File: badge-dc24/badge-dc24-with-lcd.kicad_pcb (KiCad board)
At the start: 2 copper layers, 26 parts, among them U1 ESP-12E, U2 TSOP38238, U3 74HC595

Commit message: Almost there
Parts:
- moved Program1 34.9 mm to (87.9, 116.9), turned to 180 degrees
- moved L1 22.4 mm to (86.9, 91.9)
- moved L2 22.4 mm to (84.3, 91.9)
- moved L3 22.4 mm to (81.8, 91.9)
- moved L5 22.4 mm to (76.7, 91.9)
- moved R3 22.4 mm to (76.7, 97.0)
- moved R5 22.4 mm to (81.8, 97.0)
- moved R6 22.4 mm to (84.3, 97.0)
- moved R7 22.4 mm to (86.9, 97.0)
- moved L4 22.4 mm to (79.2, 91.9)
- moved R4 22.4 mm to (79.2, 97.0)
- moved D1 21.4 mm to (91.1, 94.0)
- moved LCD1 20.9 mm to (102.4, 105.7), turned to 180 degrees
- moved U3 19.9 mm to (88.1, 81.7)
- moved Power2 19.8 mm to (77.3, 102.1)
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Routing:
- net Net-(LCD1-Pad4): track 49.2 -> 107.7 mm, vias 1 -> 0
- net Net-(Program1-Pad2): track 29.1 -> 62.7 mm
- net Net-(U1-Pad4): track 32.2 -> 52.1 mm
- net Net-(U1-Pad6): track 37.6 -> 57.5 mm
- net Net-(U1-Pad5): track 33.5 -> 52.6 mm
- net Net-(LCD1-Pad3): track 21.2 -> 37.8 mm
- net Net-(LCD1-Pad5): track 30.1 -> 43.4 mm
- net Net-(Infrared1-Pad2): track 41.5 -> 54.2 mm
- net GND: track 31.7 -> 41.4 mm
- net Net-(U1-Pad7): track 9.63 -> 18.3 mm
- net Net-(PROGRAM1-Pad1): track 28.0 -> 31.2 mm
- net Net-(RESET1-Pad2): track 13.6 -> 16.7 mm
- net Net-(L5-Pad1): track 17.5 -> 15.0 mm
- net Net-(D1-Pad4): track 6.55 -> 8.83 mm
- net Net-(D1-Pad3): track 7.08 -> 9.36 mm
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
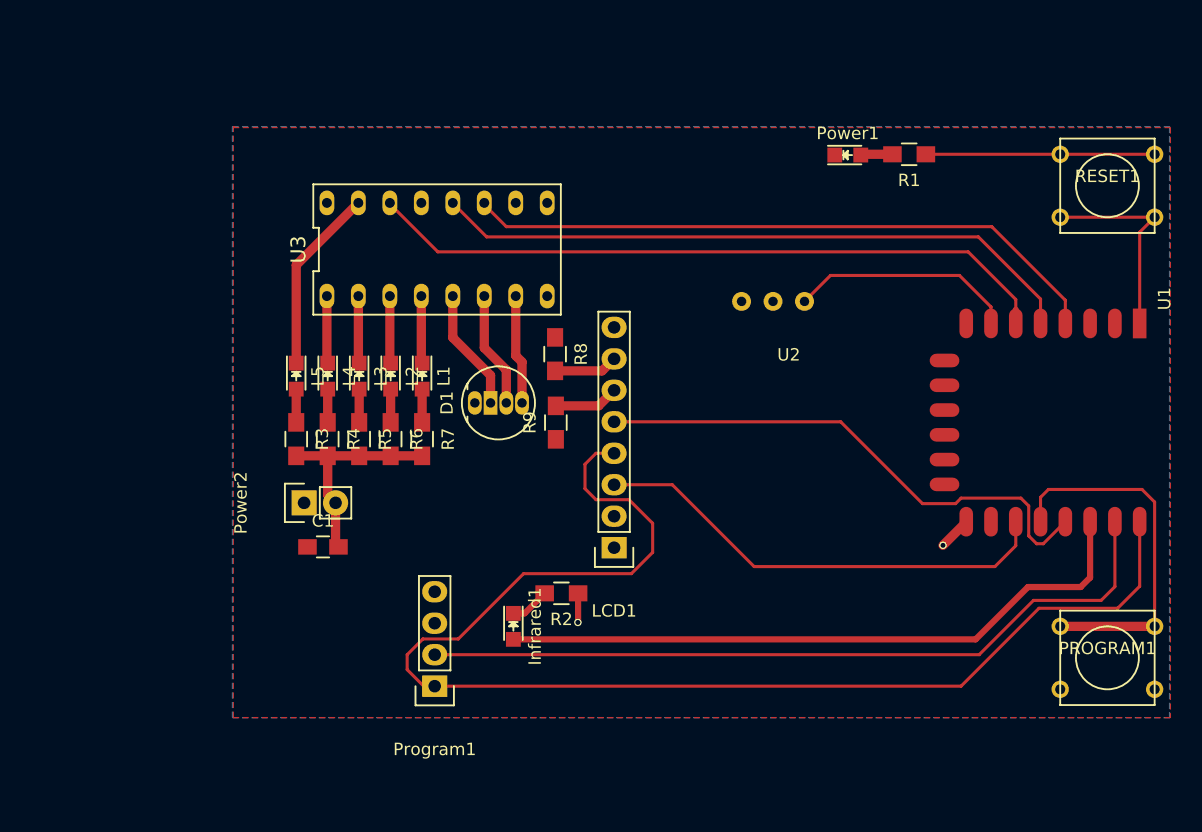
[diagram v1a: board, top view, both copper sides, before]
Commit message: Moved components out from under LCD
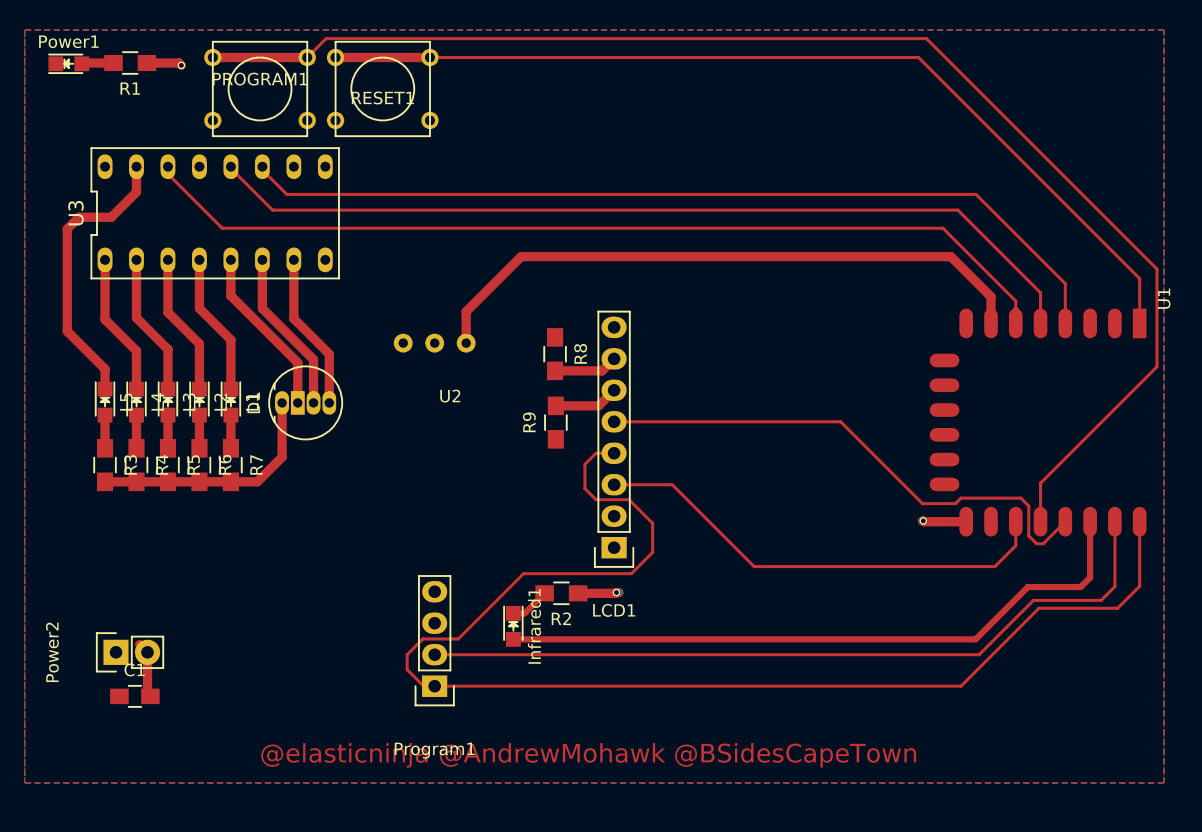
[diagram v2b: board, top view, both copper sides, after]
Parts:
- moved PROGRAM1 82.4 mm to (73.8, 68.7)
- moved Power1 63.3 mm to (58.4, 66.7)
- moved R1 63.3 mm to (63.3, 66.6)
- moved RESET1 59.0 mm to (83.7, 68.7), turned to 180 degrees
- moved U2 27.5 mm to (89.2, 93.0)
- moved C1 19.4 mm to (63.7, 117.7)
- moved Power2 19.4 mm to (62.2, 114.2)
- moved U3 18.1 mm to (70.2, 78.7)
- moved L2 15.6 mm to (68.9, 94.0)
- moved R6 15.6 mm to (68.9, 99.1)
- moved L4 15.6 mm to (63.8, 94.0)
- moved R4 15.6 mm to (63.8, 99.1)
- moved L1 15.6 mm to (71.4, 94.0)
- moved L3 15.6 mm to (66.4, 94.0)
- moved L5 15.6 mm to (61.3, 94.0)
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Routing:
- net Net-(PROGRAM1-Pad1): track 31.2 -> 110.5 mm
- net Net-(RESET1-Pad2): track 16.7 -> 75.9 mm
- net Net-(U1-Pad7): track 18.3 -> 50.2 mm
- net Net-(U1-Pad4): track 52.1 -> 72.1 mm
- net Net-(U1-Pad5): track 52.6 -> 72.1 mm
- net Net-(U1-Pad6): track 57.5 -> 76.8 mm
- net Net-(L5-Pad1): track 15.0 -> 23.1 mm
- net GND: track 41.4 -> 33.8 mm, vias 2 -> 3
- net Net-(L1-Pad1): track 5.44 -> 11.6 mm
- net Net-(L3-Pad1): track 5.44 -> 11.6 mm
- net Net-(L4-Pad1): track 5.44 -> 11.6 mm
- net Net-(L2-Pad1): track 5.44 -> 11.6 mm
- net Net-(D1-Pad3): track 9.36 -> 13.3 mm
- net Net-(D1-Pad4): track 8.83 -> 12.7 mm
- net Net-(D1-Pad2): track 9.89 -> 13.8 mm
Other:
- board text added: "@elasticninja @AndrewMohawk @BSidesCapeTown"

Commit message: Moved IR LED to the corner, for neatness' sake
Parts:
- moved Infrared1 48.0 mm to (141.4, 121.3), turned to 0 degrees
- moved R2 39.7 mm to (136.0, 121.3), turned to 0 degrees
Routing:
- net Net-(Infrared1-Pad2): track 54.2 -> 30.2 mm
- net GND: track 33.8 -> 32.2 mm
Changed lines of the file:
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@@
     (thickness 1.6)
     (drawings 5)
-    (tracks 154)
+    (tracks 152)
     (zones 0)
     (modules 26)
@@
   )
   (module LEDs:LED_0805 (layer F.Cu)
-    (at 94.234 112.0775 270)
+    (at 141.351 121.3485)
     (descr "LED 0805 smd package")
     (tags "LED 0805 SMD")
     (attr smd)
-    (fp_text reference Infrared1 (at 0 -1.75 270) (layer F.SilkS)
-      (effects (font (size 1 1) (thickness 0.15)))
-    )
-    (fp_text value LED (at 0 1.75 270) (layer F.Fab)
+    (fp_text reference Infrared1 (at 0 -1.75) (layer F.SilkS)
+      (effects (font (size 1 1) (thickness 0.15)))
+    )
+    (fp_text value LED (at 0 1.75) (layer F.Fab)
       (effects (font (size 1 1) (thickness 0.15)))
     )
@@
     (fp_line (start -1.9 0.95) (end -1.9 -0.95) (layer F.CrtYd) (width 0.05))
     (fp_line (start -1.9 -0.95) (end 1.9 -0.95) (layer F.CrtYd) (width 0.05))
-    (pad 2 smd rect (at 1.04902 0 90) (size 1.19888 1.19888) (layers F.Cu F.Paste F.Mask)
+    (pad 2 smd rect (at 1.04902 0 180) (size 1.19888 1.19888) (layers F.Cu F.Paste F.Mask)
       (net 17 "Net-(Infrared1-Pad2)"))
-    (pad 1 smd rect (at -1.04902 0 90) (size 1.19888 1.19888) (layers F.Cu F.Paste F.Mask)
+    (pad 1 smd rect (at -1.04902 0 180) (size 1.19888 1.19888) (layers F.Cu F.Paste F.Mask)
       (net 36 "Net-(Infrared1-Pad1)"))
     (model LEDs.3dshapes/LED_0805.wrl
@@
   )
   (module Resistors_SMD:R_0805_HandSoldering (layer F.Cu)
-    (at 98.1075 109.4105 180)
+    (at 135.9535 121.3485)
     (descr "Resistor SMD 0805, hand soldering")
     (tags "resistor 0805")
     (attr smd)
-    (fp_text reference R2 (at 0 -2.1 180) (layer F.SilkS)
-      (effects (font (size 1 1) (thickness 0.15)))
-    )
-    (fp_text value 100 (at 0 2.1 180) (layer F.Fab)
+    (fp_text reference R2 (at 0 -2.1) (layer F.SilkS)
+      (effects (font (size 1 1) (thickness 0.15)))
+    )
+    (fp_text value 100 (at 0 2.1) (layer F.Fab)
       (effects (font (size 1 1) (thickness 0.15)))
     )
@@
     (fp_line (start 0.6 0.875) (end -0.6 0.875) (layer F.SilkS) (width 0.15))
     (fp_line (start -0.6 -0.875) (end 0.6 -0.875) (layer F.SilkS) (width 0.15))
-    (pad 1 smd rect (at -1.35 0 180) (size 1.5 1.3) (layers F.Cu F.Paste F.Mask)
-      (net 16 GND))
-    (pad 2 smd rect (at 1.35 0 180) (size 1.5 1.3) (layers F.Cu F.Paste F.Mask)
+    (pad 1 smd rect (at -1.35 0) (size 1.5 1.3) (layers F.Cu F.Paste F.Mask)
+      (net 16 GND))
+    (pad 2 smd rect (at 1.35 0) (size 1.5 1.3) (layers F.Cu F.Paste F.Mask)
       (net 36 "Net-(Infrared1-Pad1)"))
     (model Resistors_SMD.3dshapes/R_0805_HandSoldering.wrl
@@
   (target plus (at 165.1 144.145) (size 5) (width 0.15) (layer Edge.Cuts))
   (target plus (at 67.31 144.145) (size 5) (width 0.15) (layer Edge.Cuts))
+  (segment (start 99.52102 109.88548) (end 99.5515 109.855) (width 0.25) (layer F.Cu) (net 0) (status 30))
   (segment (start 61.2775 82.5) (end 61.2775 87.3125) (width 0.75) (layer F.Cu) (net 2))
   (segment (start 63.8175 89.8525) (end 63.8175 92.93098) (width 0.75) (layer F.Cu) (net 2))
@@
   (segment (start 79.375 90.1065) (end 79.375 94.0435) (width 0.75) (layer F.Cu) (net 14))
   (segment (start 76.5175 87.249) (end 79.375 90.1065) (width 0.75) (layer F.Cu) (net 14))
-  (segment (start 99.4575 109.4105) (end 102.489 109.4105) (width 0.75) (layer F.Cu) (net 16) (status 400000))
-  (segment (start 102.5525 109.347) (end 102.743 109.347) (width 0.75) (layer B.Cu) (net 16))
-  (via (at 102.5525 109.347) (size 0.6) (drill 0.4) (layers F.Cu B.Cu) (net 16))
-  (segment (start 102.489 109.4105) (end 102.5525 109.347) (width 0.75) (layer F.Cu) (net 16))
+  (segment (start 134.6035 121.3485) (end 132.842 121.3485) (width 0.75) (layer F.Cu) (net 16) (status 400000))
+  (via (at 132.842 121.3485) (size 0.6) (drill 0.4) (layers F.Cu B.Cu) (net 16))
   (segment (start 64.6595 66.6115) (end 67.2465 66.6115) (width 0.75) (layer F.Cu) (net 16))
   (via (at 67.437 66.802) (size 0.6) (drill 0.4) (layers F.Cu B.Cu) (net 16))
@@
   (segment (start 63.8175 100.41) (end 66.3575 100.41) (width 0.75) (layer F.Cu) (net 16) (status 30))
   (segment (start 61.2775 100.41) (end 63.8175 100.41) (width 0.75) (layer F.Cu) (net 16) (status 30))
-  (segment (start 99.52102 109.88548) (end 99.5515 109.855) (width 0.25) (layer F.Cu) (net 16) (status 30))
-  (segment (start 94.234 113.12652) (end 131.53898 113.12652) (width 0.5) (layer F.Cu) (net 17) (status 10))
-  (segment (start 140.78 108.14) (end 140.78 103.63) (width 0.5) (layer F.Cu) (net 17) (status 20))
-  (segment (start 140.0175 108.9025) (end 140.78 108.14) (width 0.5) (layer F.Cu) (net 17))
-  (segment (start 135.763 108.9025) (end 140.0175 108.9025) (width 0.5) (layer F.Cu) (net 17))
-  (segment (start 131.53898 113.12652) (end 135.763 108.9025) (width 0.5) (layer F.Cu) (net 17))
-  (segment (start 140.78 104.711) (end 140.78 103.63) (width 0.25) (layer F.Cu) (net 17) (status 30))
+  (segment (start 140.78 103.63) (end 140.78 102.1075) (width 0.75) (layer F.Cu) (net 17) (status 400000))
+  (segment (start 144.4625 121.3485) (end 142.40002 121.3485) (width 0.75) (layer F.Cu) (net 17) (status 800000))
+  (segment (start 146.177 119.634) (end 144.4625 121.3485) (width 0.75) (layer F.Cu) (net 17))
+  (segment (start 146.177 101.6635) (end 146.177 119.634) (width 0.75) (layer F.Cu) (net 17))
+  (segment (start 145.3515 100.838) (end 146.177 101.6635) (width 0.75) (layer F.Cu) (net 17))
+  (segment (start 142.0495 100.838) (end 145.3515 100.838) (width 0.75) (layer F.Cu) (net 17))
+  (segment (start 140.78 102.1075) (end 142.0495 100.838) (width 0.75) (layer F.Cu) (net 17))
   (segment (start 68.8975 95.02902) (end 68.8975 97.71) (width 0.75) (layer F.Cu) (net 18) (status 30))
   (segment (start 66.3575 95.02902) (end 66.3575 97.71) (width 0.75) (layer F.Cu) (net 19) (status 30))
@@
   (segment (start 94.869 82.2325) (end 129.54 82.2325) (width 0.75) (layer F.Cu) (net 34))
   (segment (start 90.424 86.6775) (end 94.869 82.2325) (width 0.75) (layer F.Cu) (net 34))
-  (segment (start 94.234 111.02848) (end 95.13952 111.02848) (width 0.5) (layer F.Cu) (net 36) (status 10))
-  (segment (start 95.13952 111.02848) (end 96.7575 109.4105) (width 0.5) (layer F.Cu) (net 36) (status 20))
+  (segment (start 140.30198 121.3485) (end 137.3035 121.3485) (width 0.75) (layer F.Cu) (net 36) (status C00000))
   (segment (start 134.78 103.63) (end 134.78 105.5675) (width 0.25) (layer F.Cu) (net 37) (status 10))
   (segment (start 107.061 100.6475) (end 102.362 100.6475) (width 0.25) (layer F.Cu) (net 37) (status 20))

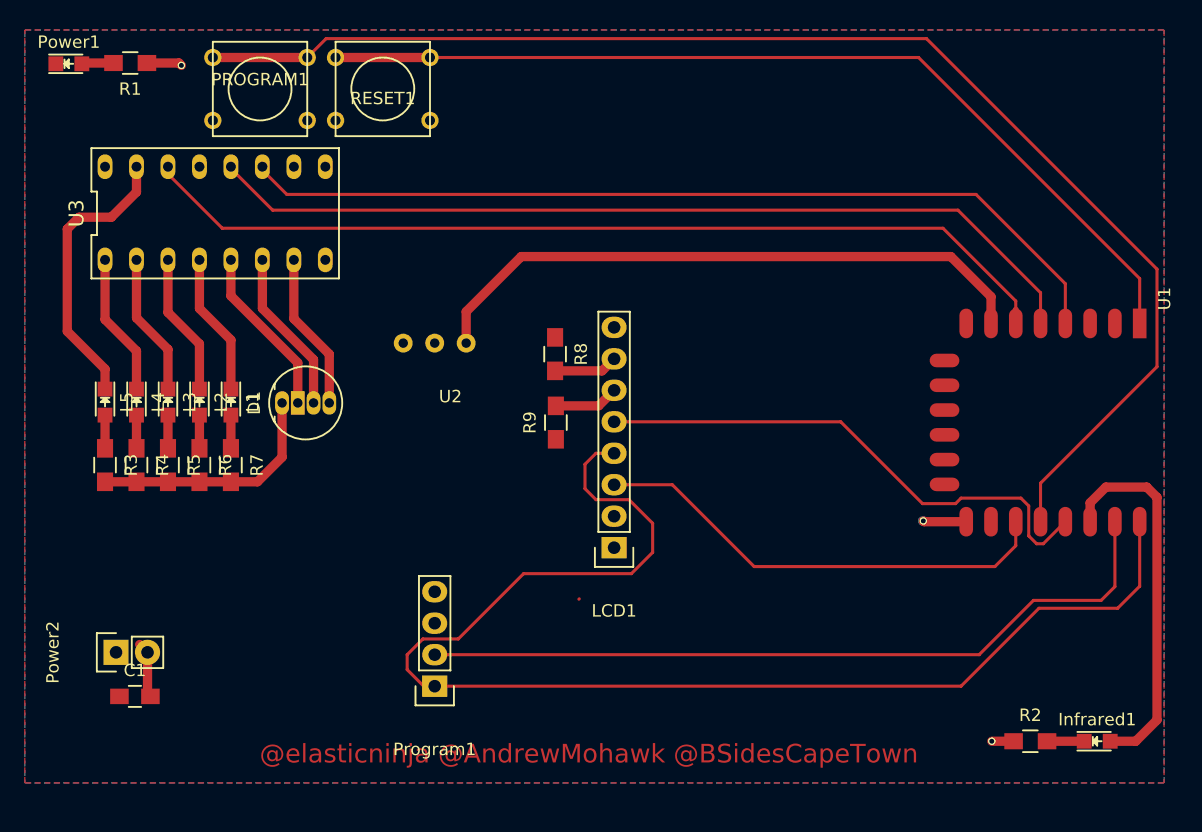
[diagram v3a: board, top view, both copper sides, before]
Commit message: Moved reg marks + fixed temp tx wire problem
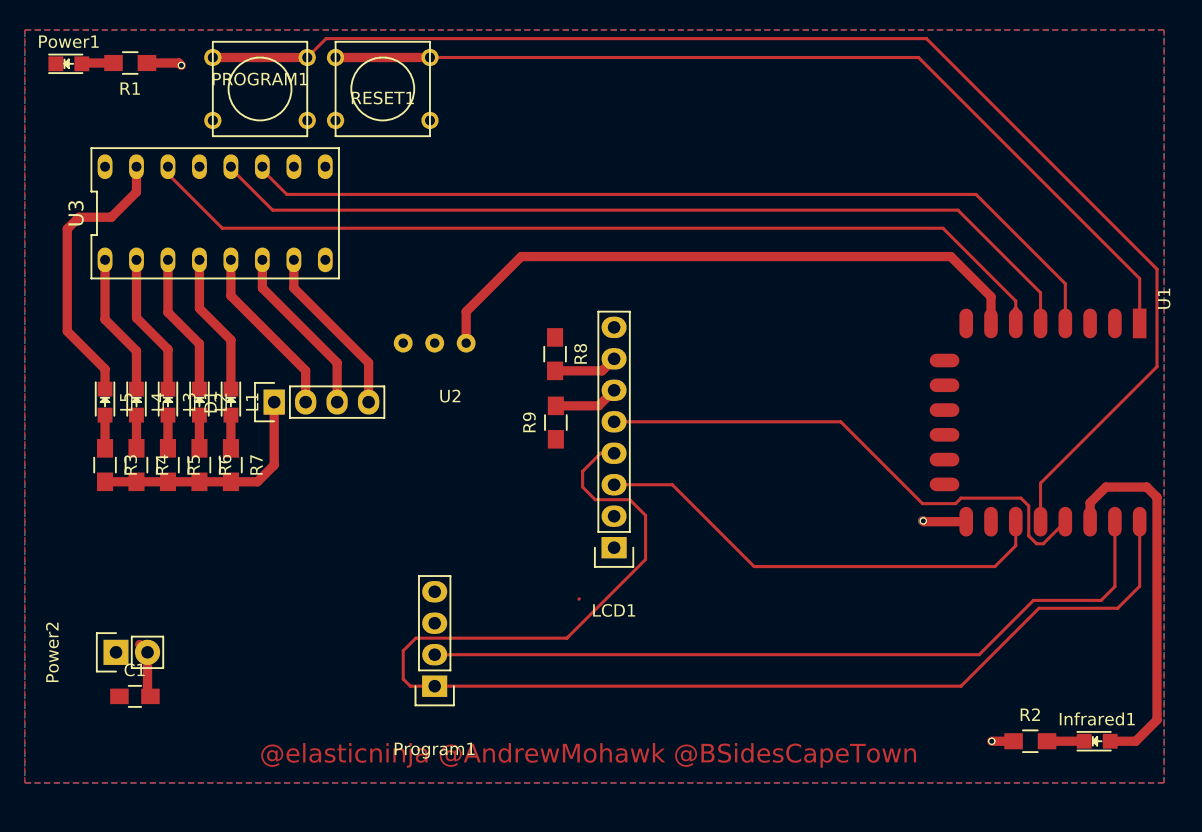
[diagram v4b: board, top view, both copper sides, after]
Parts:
- D1: footprint LEDs:LED-RGB-5MM_Common_Cathode -> Pin_Headers:Pin_Header_Straight_1x04
- moved D1 0.64 mm to (74.9, 94.0)
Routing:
- net Net-(LCD1-Pad4): track 107.7 -> 109.4 mm
- net Net-(D1-Pad4): track 12.7 -> 14.0 mm
- net Net-(D1-Pad3): track 13.3 -> 14.0 mm

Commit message: New design based on learnings from first design
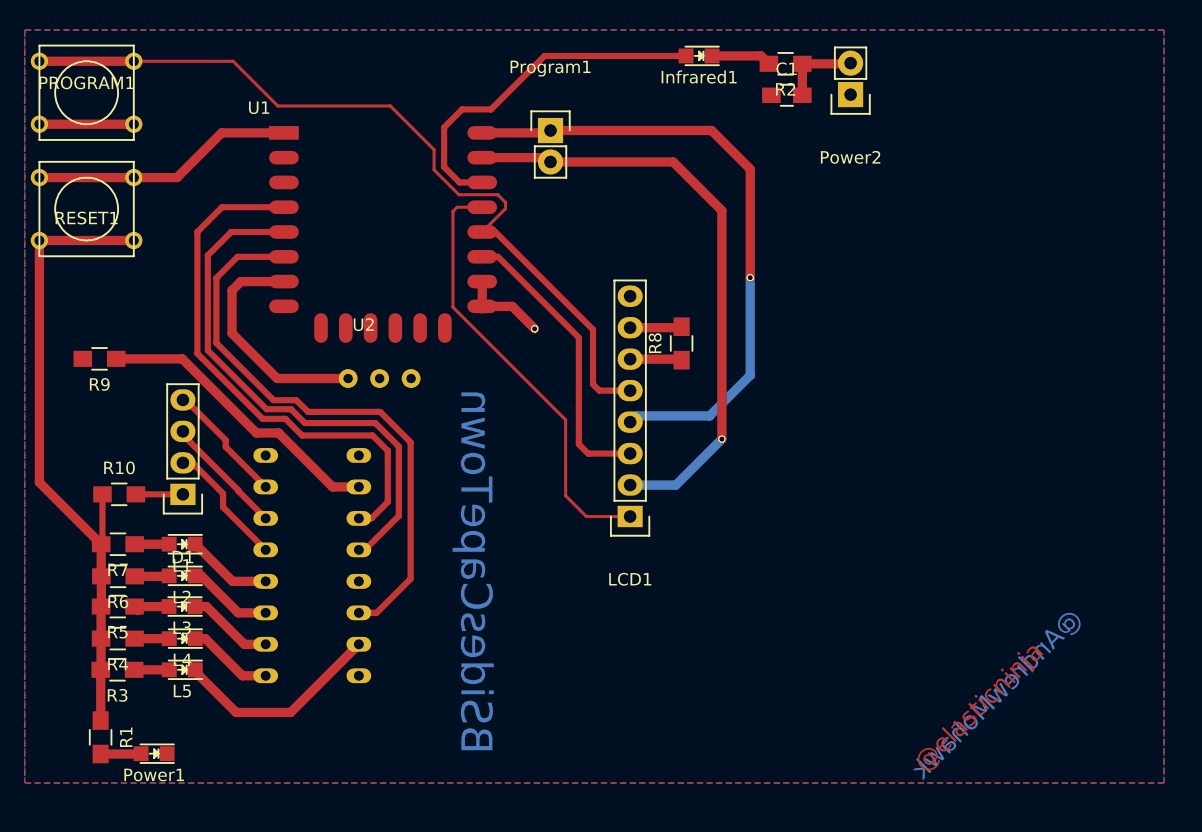
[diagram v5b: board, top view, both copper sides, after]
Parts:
- added R10: 100, Resistors_SMD:R_0805_HandSoldering, F.Cu at (62.4, 101.4)
- Program1: value CONN_01X04 -> CONN_01X02; footprint Pin_Headers:Pin_Header_Straight_1x04 -> Pin_Headers:Pin_Header_Straight_1x02
- U3: moved to B.Cu
- moved Power2 74.4 mm to (121.5, 69.2), turned to 180 degrees
- moved C1 71.6 mm to (116.3, 69.2)
- moved U1 70.8 mm to (75.7, 72.3), turned to 0 degrees
- moved Infrared1 64.0 mm to (109.2, 66.0), turned to 180 degrees
- moved R2 58.1 mm to (116.2, 66.7), turned to 180 degrees
- moved Power1 56.1 mm to (65.2, 122.4), turned to 180 degrees
- moved R1 54.5 mm to (60.9, 121.0), turned to 270 degrees
- moved Program1 45.8 mm to (97.2, 72.1), turned to 0 degrees
- moved R9 37.2 mm to (60.8, 90.5), turned to 180 degrees
- moved U3 29.5 mm to (78.0, 107.2), turned to 90 degrees
- moved RESET1 25.8 mm to (59.8, 78.4)
- moved L5 22.5 mm to (67.5, 115.6), turned to 180 degrees
- moved L4 19.4 mm to (67.5, 113.1), turned to 180 degrees
- moved R3 16.6 mm to (62.3, 115.6), turned to 180 degrees
- moved L3 16.5 mm to (67.5, 110.5), turned to 180 degrees
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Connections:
- D1 pad 1: GND -> Net-(D1-Pad1)
- LCD1 pad 1: GND -> Net-(LCD1-Pad1)
- LCD1 pad 2: +3V3 -> Net-(LCD1-Pad2)
- LCD1 pad 6: Net-(LCD1-Pad6) -> +3V3
- PROGRAM1 pad 1: Net-(PROGRAM1-Pad1) -> Net-(LCD1-Pad5)
- Program1 pad 2: Net-(Program1-Pad2) -> Net-(LCD1-Pad2)
- R9 pad 1: +3V3 -> Net-(R9-Pad1)
- R9 pad 2: Net-(LCD1-Pad6) -> +3V3
- U1 pad 16: Net-(U1-Pad16) -> GND
- U1 pad 18: Net-(PROGRAM1-Pad1) -> Net-(LCD1-Pad5)
- U1 pad 19: Net-(LCD1-Pad5) -> Net-(LCD1-Pad1)
- U1 pad 21: Net-(Program1-Pad2) -> Net-(LCD1-Pad2)
- U1 pad 3: Net-(U1-Pad3) -> +3V3
- U3 pad 10: Net-(U3-Pad10) -> Net-(R9-Pad1)
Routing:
- net Net-(PROGRAM1-Pad1): track 110.5 -> 0.00 mm
- net Net-(Program1-Pad2): track 62.7 -> 0.00 mm
- net Net-(LCD1-Pad4): track 109.4 -> 50.9 mm, vias 0 -> 1
- net Net-(RESET1-Pad2): track 75.9 -> 21.2 mm
- net Net-(LCD1-Pad2): track 0.00 -> 48.5 mm, vias 0 -> 1
- net GND: track 32.0 -> 73.9 mm, vias 3 -> 1
- net Net-(LCD1-Pad1): track 0.00 -> 35.1 mm
- net Net-(U1-Pad7): track 50.2 -> 18.8 mm
- net Net-(U1-Pad6): track 76.8 -> 47.7 mm
- net Net-(U1-Pad4): track 72.1 -> 43.3 mm
- net Net-(U1-Pad5): track 72.1 -> 43.9 mm
- net Net-(R9-Pad1): track 0.00 -> 23.9 mm
- net Net-(LCD1-Pad5): track 43.4 -> 66.3 mm
- net Net-(LCD1-Pad3): track 37.8 -> 23.6 mm
- net Net-(L5-Pad1): track 23.1 -> 17.0 mm
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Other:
- board text added: "@AndrewMohawk"
- board text added: "@elasticninja"
- board text added: "BSidesCapeTown"
- board text removed: "@elasticninja @AndrewMohawk @BSidesCapeTown"
